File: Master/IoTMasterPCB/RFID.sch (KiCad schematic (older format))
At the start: 0 parts

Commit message: Added some components for Master Board schematic.
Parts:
- added IC?: CLRC66303HNY, Personal_ICs:CLRC66303HNY, symbol Personal_ICs:CLRC66303HNY
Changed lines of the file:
@@
 $Descr A4 11693 8268
 encoding utf-8
-Sheet 1 6
+Sheet 4 6
 Title "IoT Master Board"
 Date "2020-11-28"
@@
 Comment4 ""
 $EndDescr
+$Comp
+L Personal_ICs:CLRC66303HNY IC?
+U 1 1 5FCB29B8
+P 4850 3350
+F 0 "IC?" H 6694 3196 50  0000 L CNN
+F 1 "CLRC66303HNY" H 6694 3105 50  0000 L CNN
+F 2 "Personal_ICs:CLRC66303HNY" H 6500 4150 50  0001 L CNN
+F 3 "http://www.nxp.com/docs/en/data-sheet/SLRC610.pdf" H 6500 4050 50  0001 L CNN
+F 4 "NXP - CLRC66303HNY - MULTI-PROTOCOL NFC FRONTEND, HVQFN-32" H 6500 3950 50  0001 L CNN "Description"
+F 5 "1" H 6500 3850 50  0001 L CNN "Height"
+F 6 "NXP" H 6500 3750 50  0001 L CNN "Manufacturer_Name"
+F 7 "CLRC66303HNY" H 6500 3650 50  0001 L CNN "Manufacturer_Part_Number"
+F 8 "CLRC66303HNY" H 6500 3550 50  0001 L CNN "Arrow Part Number"
+F 9 "https://www.arrow.com/en/products/clrc66303hny/nxp-semiconductors" H 6500 3450 50  0001 L CNN "Arrow Price/Stock"
+F 10 "771-CLRC66303HNY" H 6500 3350 50  0001 L CNN "Mouser Part Number"
+F 11 "https://www.mouser.co.uk/ProductDetail/NXP-Semiconductors/CLRC66303HNY?qs=gH1BdSMZm8V9YDgcadCntw%3D%3D" H 6500 3250 50  0001 L CNN "Mouser Price/Stock"
+	1    4850 3350
+	1    0    0    -1
+$EndComp
 $EndSCHEMATC

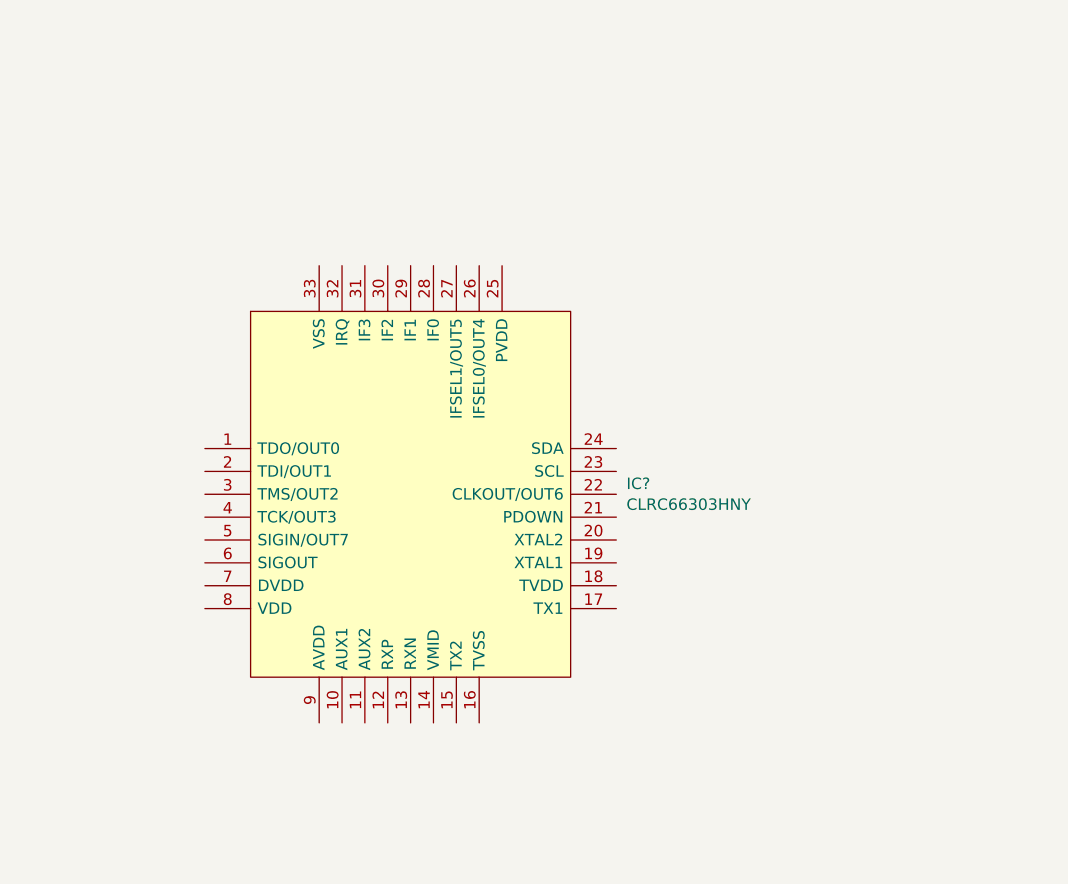
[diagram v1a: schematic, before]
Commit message: Added flash storage, work on RFID front-end.
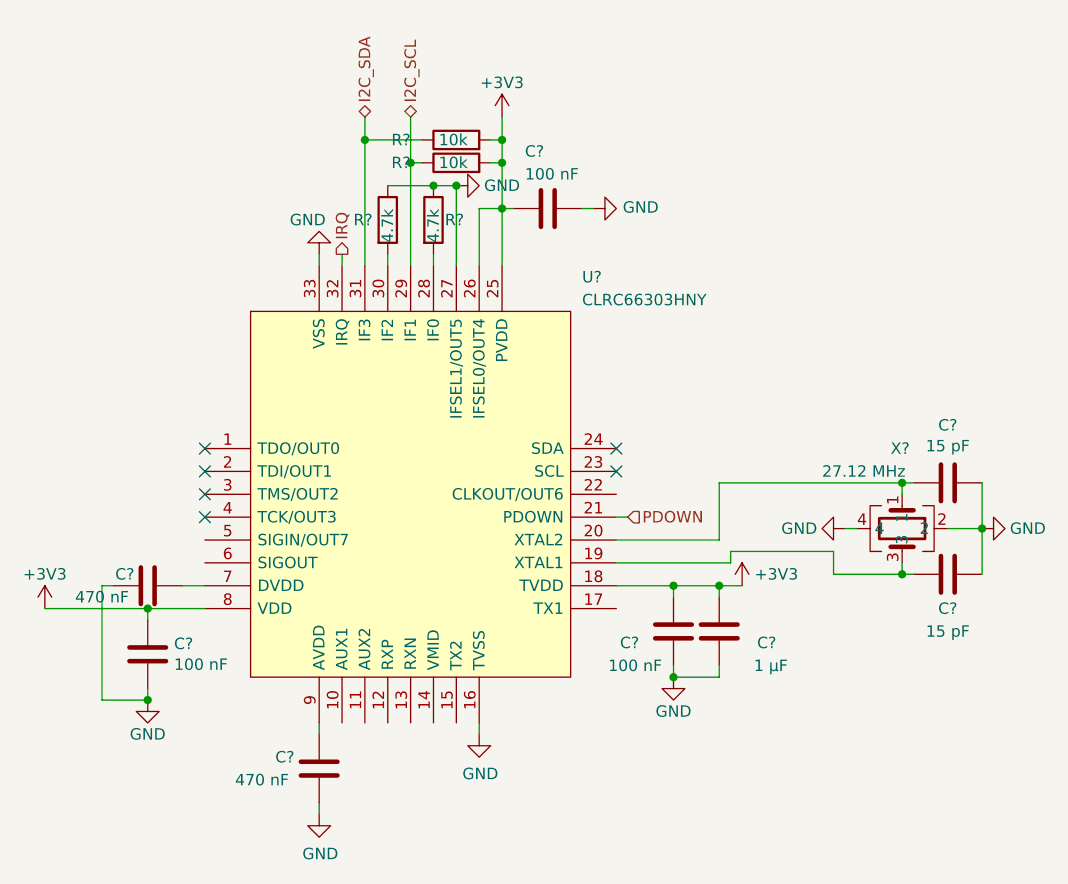
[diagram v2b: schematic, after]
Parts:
- added C? (x3): 100 nF, Capacitor_SMD:C_0603_1608Metric, symbol Device:C
- added C?: 1 µF, Capacitor_SMD:C_0603_1608Metric, symbol Device:C
- added C? (x2): 470 nF, Capacitor_SMD:C_0603_1608Metric, symbol Device:C
- added C? (x2): 15 pF, Capacitor_SMD:C_0603_1608Metric, symbol Device:C
- added R? (x2): 10k, Resistor_SMD:R_0603_1608Metric, symbol Device:R
- added R? (x2): 4.7k, Resistor_SMD:R_0603_1608Metric, symbol Device:R
- added X?: 27.12 MHz, Personal_Actives:ECS27121037AGNTR, symbol Personal_Actives:ECS-271.2-10-37-AGN-TR
- gave numbers to parts that had none: 1
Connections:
- net GND: now reaches U?.16 (TVSS)
- net GND: now also U?.27 (IFSEL1/OUT5), U?.33 (VSS), C?.1, C?.1, C?.1, C?.1, C?.1, C?.1, C?.2, C?.2, R?.1, R?.1, X?.2, X?.4
- net +3V3: now reaches U?.18 (TVDD)
- net +3V3: now also U?.25 (PVDD), U?.26 (IFSEL0/OUT4), U?.8 (VDD), C?.1, C?.2, C?.2, C?.2, R?.2, R?.2
- net at U?.19 (XTAL1): now also C?.2, X?.3
- net at U?.20 (XTAL2): now also C?.2, X?.1
- net PDOWN: now reaches U?.21 (PDOWN)
- net at U?.28 (IF0): now also R?.2
- net I2C_SCL: now reaches U?.29 (IF1)
- net I2C_SCL: now also R?.1
- net at U?.30 (IF2): now also R?.2
- net I2C_SDA: now reaches U?.31 (IF3)
- net I2C_SDA: now also R?.1
- net IRQ: now reaches U?.32 (IRQ)
- net at U?.7 (DVDD): now also C?.1
- net at U?.9 (AVDD): now also C?.2
- no-connect marks 0 -> 6

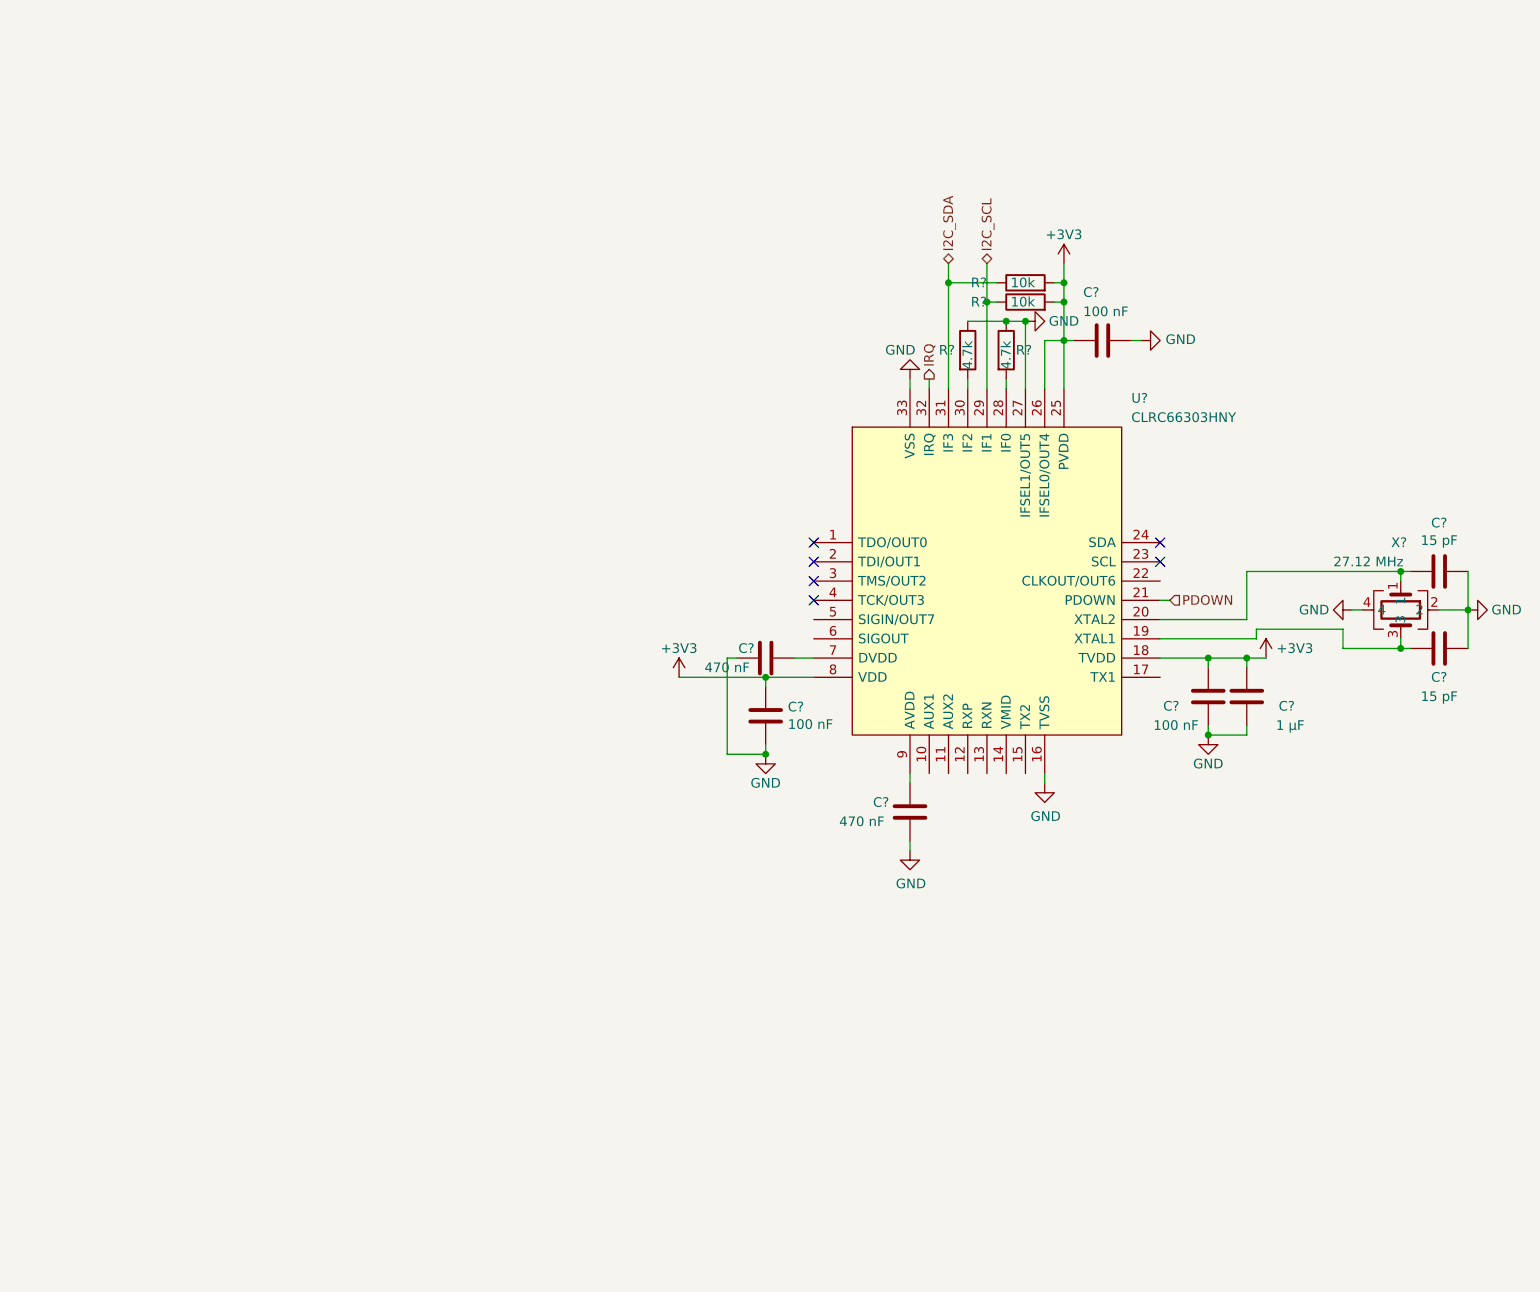
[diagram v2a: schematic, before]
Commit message: Finished RFID module sans antenna footprint. Added KSZ8081MNX and hierarchial connections.
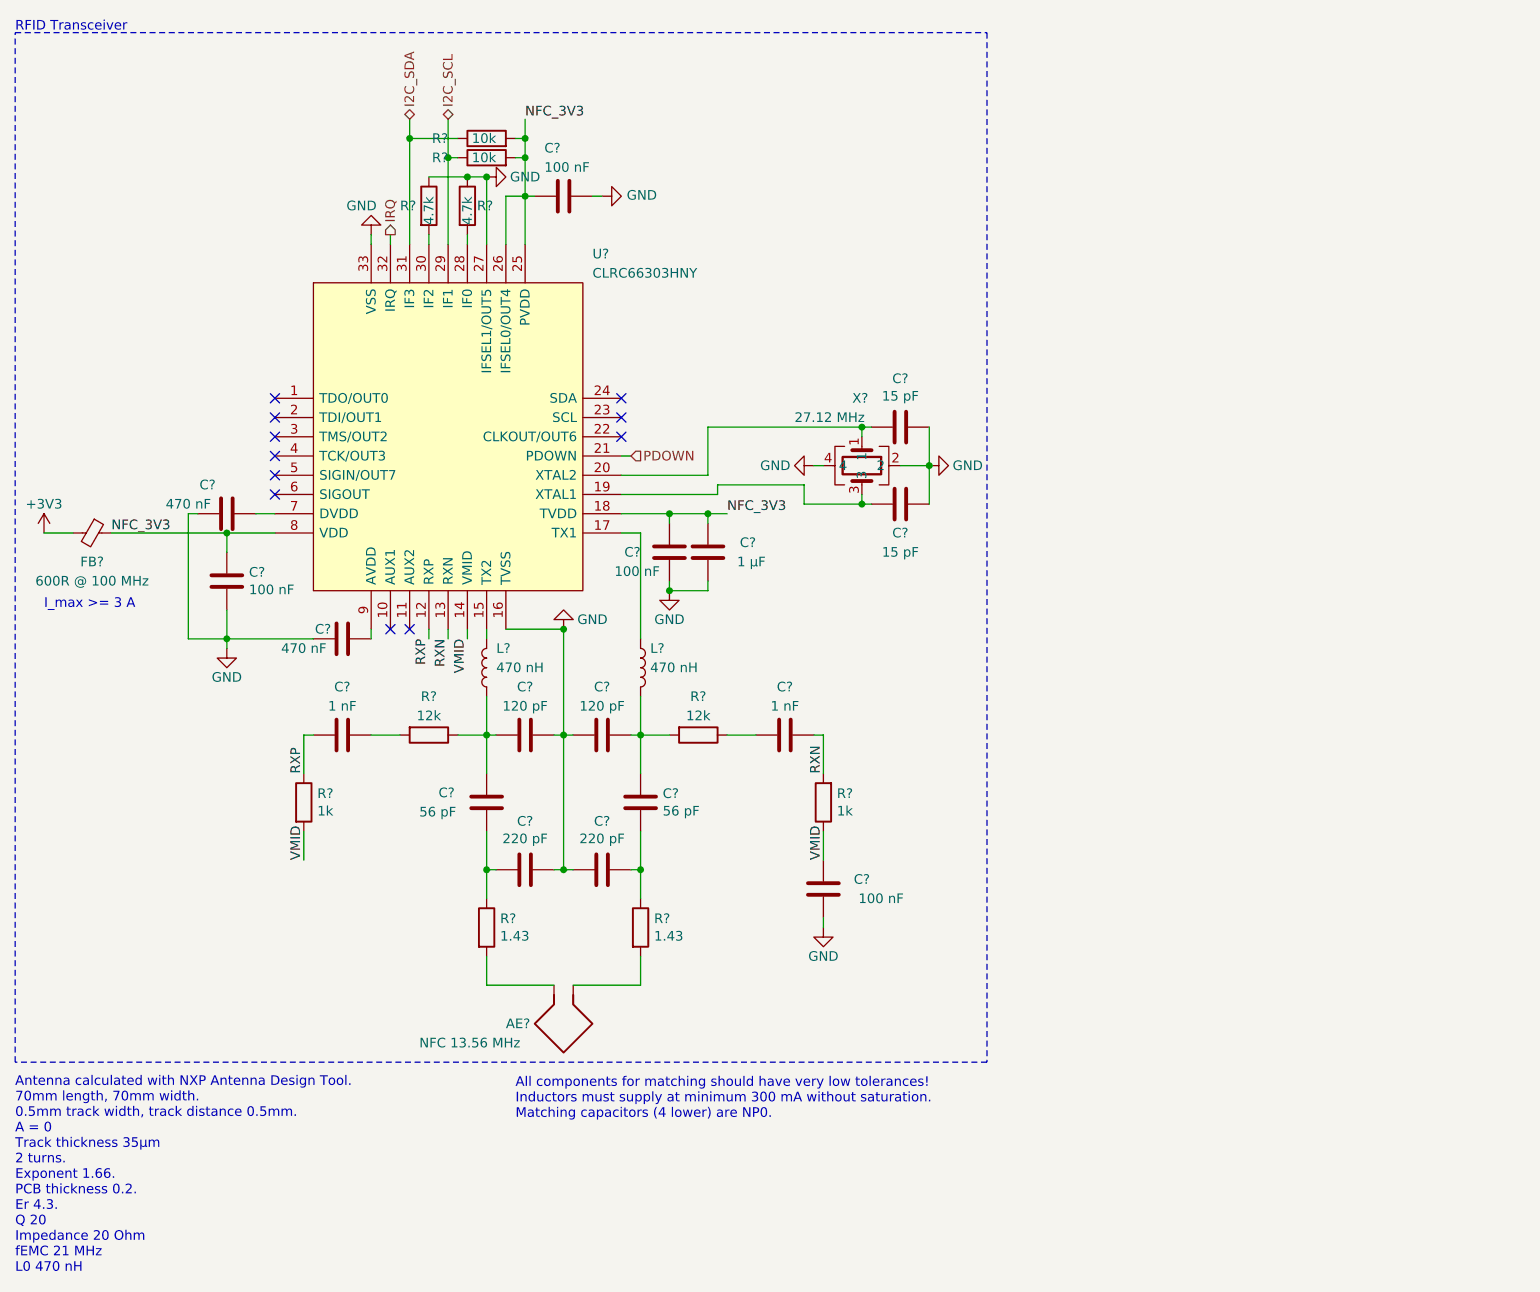
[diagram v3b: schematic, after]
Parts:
- added AE?: NFC 13.56 MHz, symbol Device:Antenna_Loop
- added C? (x2): 120 pF, symbol Device:C
- added C? (x2): 56 pF, symbol Device:C
- added C? (x2): 220 pF, symbol Device:C
- added C? (x2): 1 nF, symbol Device:C
- added C?: 100 nF, symbol Device:C
- added FB?: 600R @ 100 MHz, symbol Device:Ferrite_Bead_Small
- added L? (x2): 470 nH, symbol Device:L
- added R? (x2): 1.43, symbol Device:R
- added R? (x2): 12k, symbol Device:R
- added R? (x2): 1k, symbol Device:R
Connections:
- net +3V3: now also FB?.2; no longer C?.1, C?.2, C?.2, C?.2, R?.2, R?.2, U?.18 (TVDD), U?.25 (PVDD), U?.26 (IFSEL0/OUT4), U?.8 (VDD)
- net GND: now also C?.1, C?.1, C?.2, C?.2, C?.2
- net RXP: now reaches U?.12 (RXP)
- net RXP: now also C?.1, R?.1
- net RXN: now reaches U?.13 (RXN)
- net RXN: now also C?.1, R?.2
- net VMID: now reaches U?.14 (VMID)
- net VMID: now also C?.1, R?.1, R?.2
- net at U?.15 (TX2): now also L?.2
- net at U?.17 (TX1): now also L?.1
- new net: C?.1, C?.2, L?.2, R?.2
- new net: C?.2, C?.2, L?.1, R?.1
- new net: C?.1, C?.1, R?.1
- new net: C?.1, C?.2, R?.1
- new net: AE?.1, R?.2
- new net: AE?.2, R?.2
- new net: C?.2, R?.1
- new net: C?.2, R?.2
- new net NFC_3V3: C?.1, C?.2, C?.2, C?.2, FB?.1, R?.2, R?.2, U?.18 (TVDD), U?.25 (PVDD), U?.26 (IFSEL0/OUT4), U?.8 (VDD)
- no-connect marks 6 -> 11
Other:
- note added: "All components for matching should have very low tolerances!\nInductors must supply at minimum 300 mA without saturation.\nMatching capacitors (4 lower) are NP0."
- note added: "Antenna calculated with NXP Antenna Design Tool.\n70mm length, 70mm width. \n0.5mm track width, track distance 0.5mm.\nA = 0\nTrack thickness 35µm\n2 turns.\nExponent 1.66.\nPCB thickness 0.2.\nEr 4.3.\nQ 20\nImpedance 20 Ohm\nfEMC 21 MHz\nL0 470 nH"
- note added: "I_max >= 3 A"
- note added: "RFID Transceiver"
- moved on the sheet: C?, R?, U?, X?

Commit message: Finished RFID and Ethernet circuits.
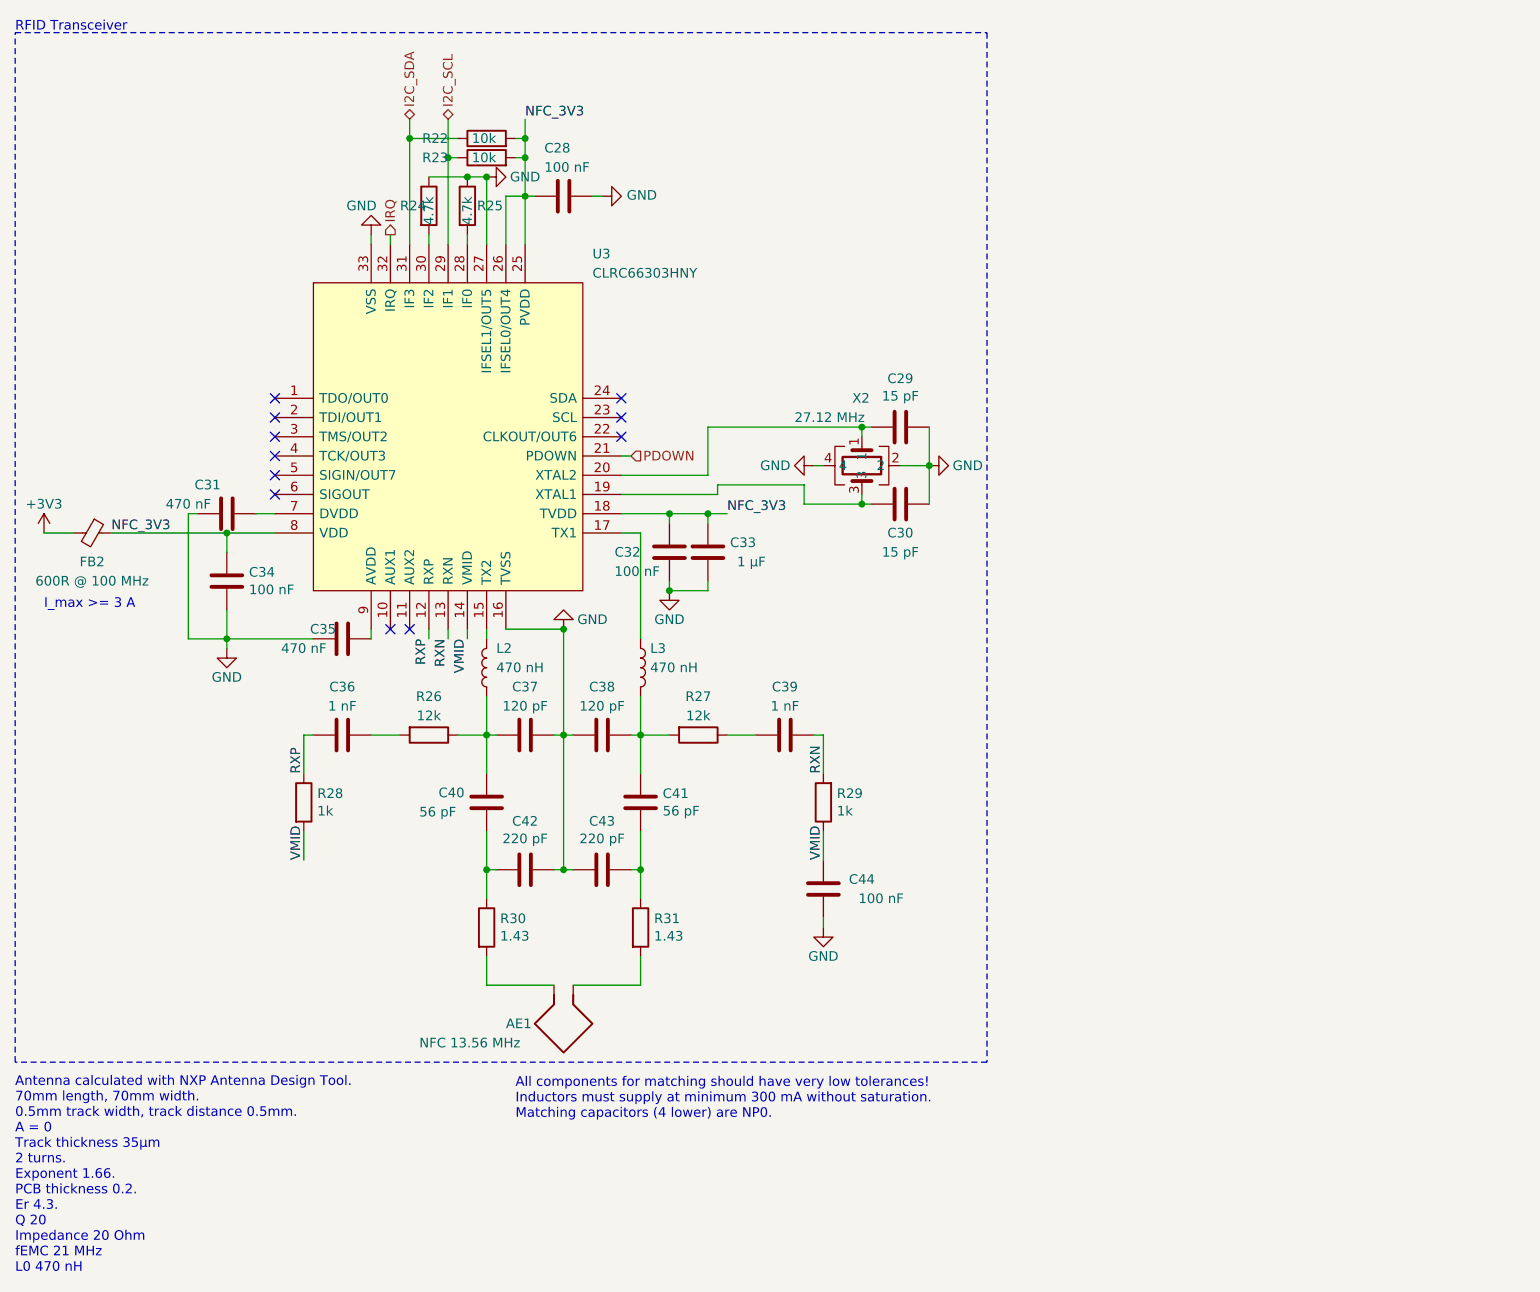
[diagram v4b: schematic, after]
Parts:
- AE1: renamed from AE?; footprint (none) -> Personal_Misc:NXP_NFC_13.56MHz
- C36, C37, C38, C39, C40, C41, C42, C43, C44: renamed from C?; footprint (none) -> Capacitor_SMD:C_0603_1608Metric
- FB2: renamed from FB?; footprint (none) -> Inductor_SMD:L_1210_3225Metric
- L2, L3: renamed from L?; footprint (none) -> Personal_Passives:SRN2512R47M
- R26, R27, R28, R29, R30, R31: renamed from R?; footprint (none) -> Resistor_SMD:R_0603_1608Metric
- gave numbers to parts that had none: 14
